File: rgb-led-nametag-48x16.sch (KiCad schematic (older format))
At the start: 1 part, among them J1 USB_C_Receptacle_USB2.0

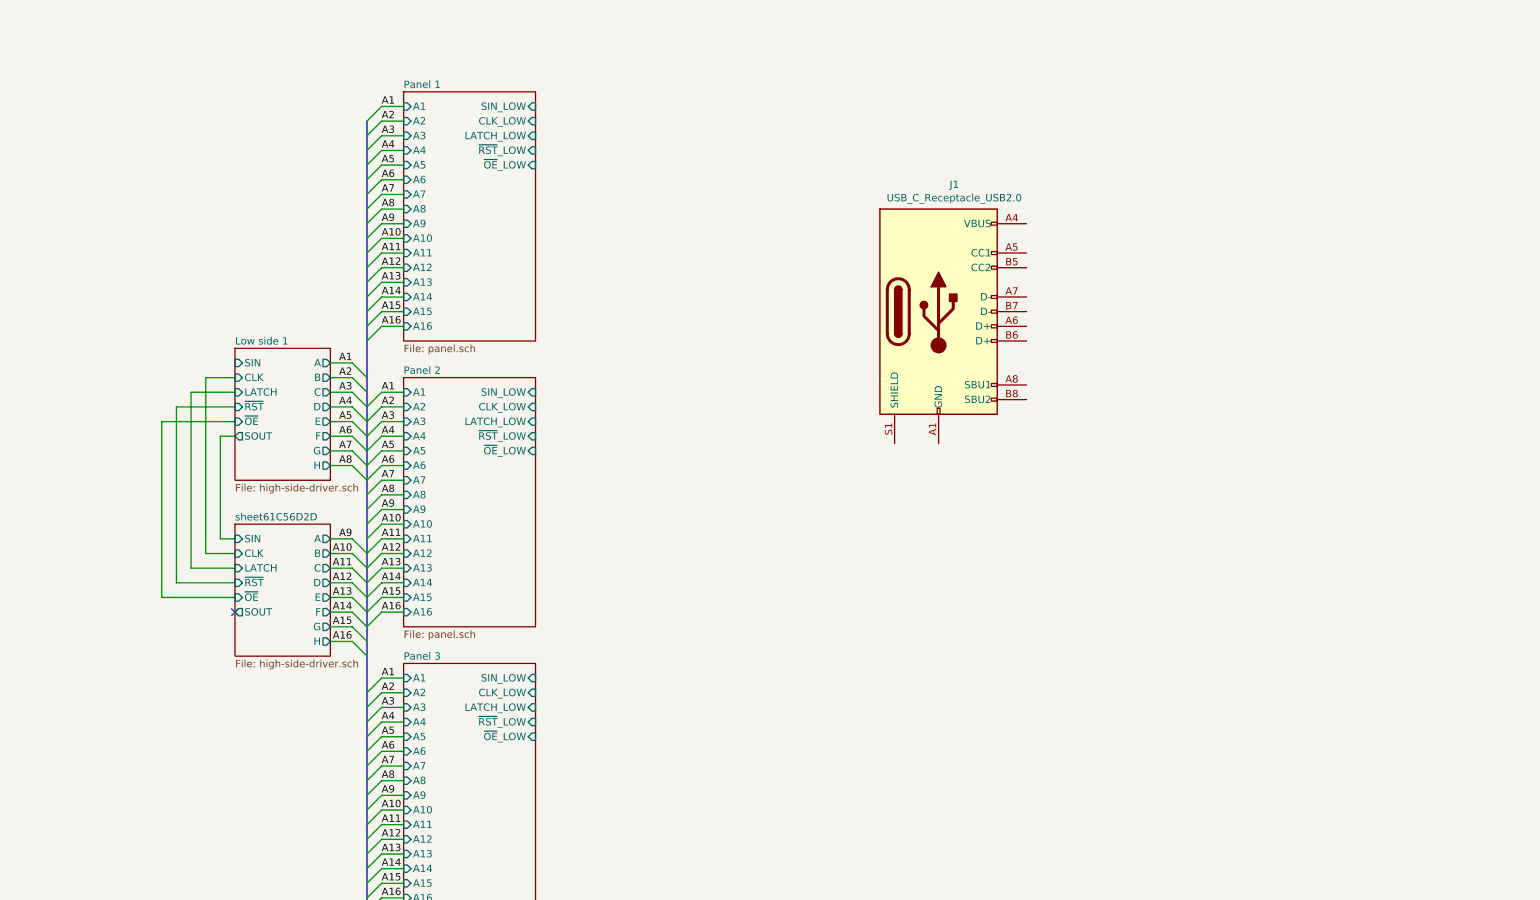
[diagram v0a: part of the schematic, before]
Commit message: Finish STM32 digital interface assignment
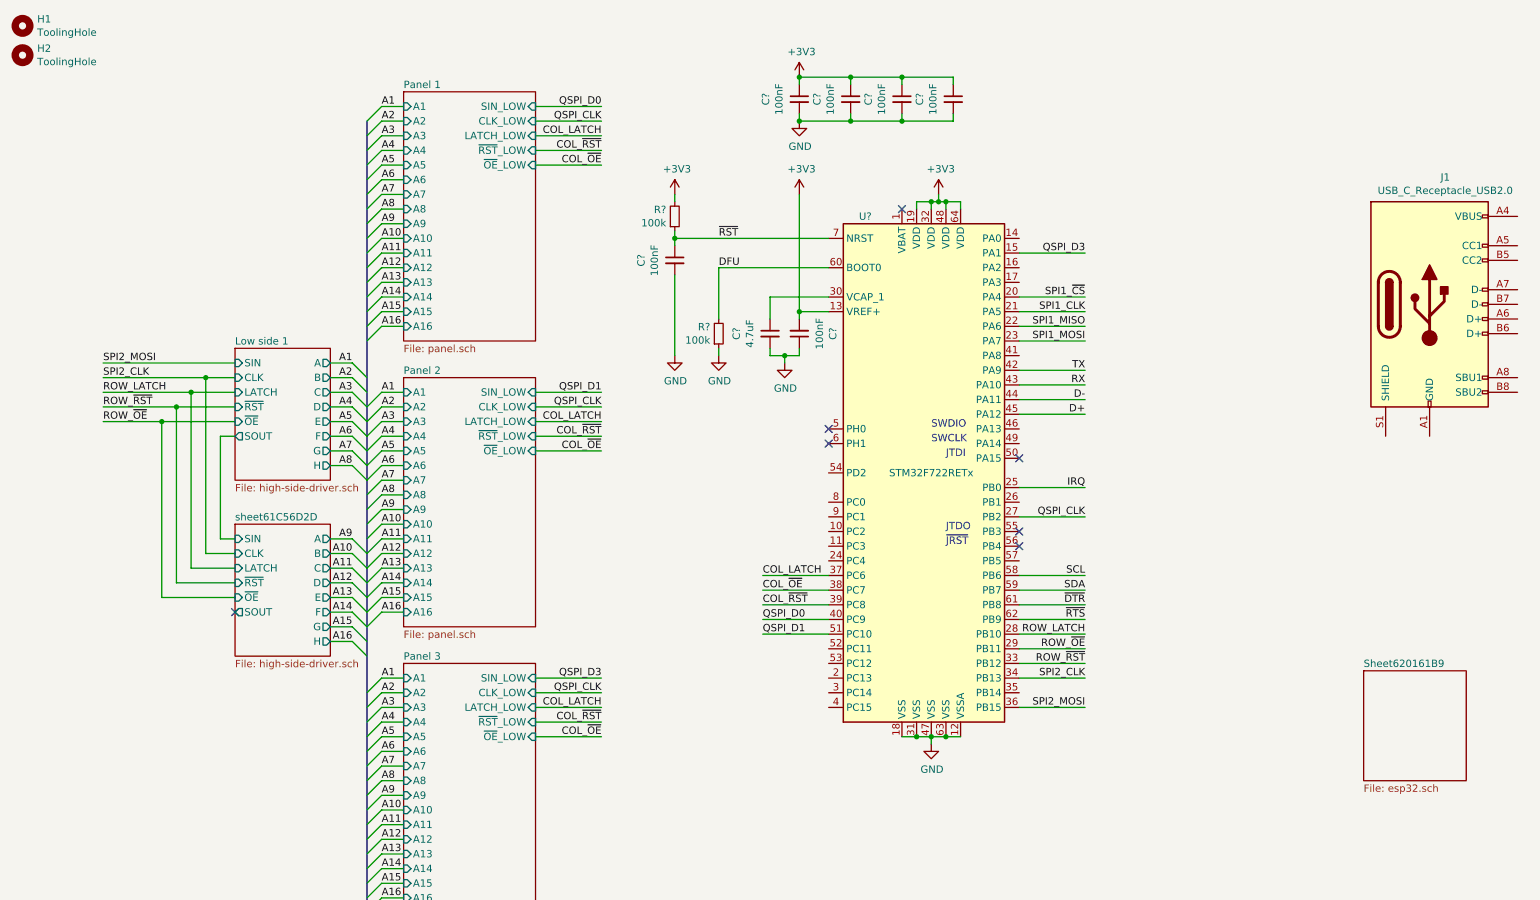
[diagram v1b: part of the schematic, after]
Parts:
- added C?: 4.7uF, Capacitor_SMD:C_0402_1005Metric, symbol Device:C_Small
- added C? (x6): 100nF, Capacitor_SMD:C_0402_1005Metric, symbol Device:C_Small
- added H1, H2: ToolingHole, ToolingHole:ToolingHole_JLCSMT, symbol Mechanical:MountingHole
- added R? (x2): 100k, Resistor_SMD:R_0402_1005Metric, symbol Device:R_Small
- added U?: STM32F722RETx, Package_QFP:LQFP-64_10x10mm_P0.5mm, symbol MCU_ST_STM32F7:STM32F722RETx
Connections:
- new net: C?.1, U?.30 (VCAP_1)
- new net +3V3: C?.1, C?.1, C?.1, C?.1, C?.2, R?.2, U?.13 (VREF+), U?.19 (VDD), U?.32 (VDD), U?.48 (VDD), U?.64 (VDD)
- new net COL_LATCH: U?.37 (PC6)
- new net COL_~OE: U?.38 (PC7)
- new net COL_~RST: U?.39 (PC8)
- new net D+: U?.45 (PA12)
- new net D-: U?.44 (PA11)
- new net DFU: R?.2, U?.60 (BOOT0)
- new net GND: C?.1, C?.2, C?.2, C?.2, C?.2, C?.2, C?.2, R?.1, U?.12 (VSSA), U?.18 (VSS), U?.31 (VSS), U?.47 (VSS), U?.63 (VSS)
- new net IRQ: U?.25 (PB0)
- new net QSPI_CLK: U?.27 (PB2)
- new net QSPI_D0: U?.40 (PC9)
- new net QSPI_D1: U?.51 (PC10)
- new net QSPI_D3: U?.15 (PA1)
- new net ROW_LATCH: U?.28 (PB10)
- new net ROW_~OE: U?.29 (PB11)
- new net ROW_~RST: U?.33 (PB12)
- new net RX: U?.43 (PA10)
- new net SCL: U?.58 (PB6)
- new net SDA: U?.59 (PB7)
- new net SPI1_CLK: U?.21 (PA5)
- new net SPI1_MISO: U?.22 (PA6)
- new net SPI1_MOSI: U?.23 (PA7)
- new net SPI1_~CS: U?.20 (PA4)
- new net SPI2_CLK: U?.34 (PB13)
- new net SPI2_MOSI: U?.36 (PB15)
- new net TX: U?.42 (PA9)
- new net ~DTR: U?.61 (PB8)
- new net ~RST: C?.1, R?.1, U?.7 (NRST)
- new net ~RTS: U?.62 (PB9)
- no-connect marks 1 -> 7
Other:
- note added: "JTDI"
- note added: "JTDO"
- note added: "SWCLK"
- note added: "SWDIO"
- note added: "~JRST"
- moved on the sheet: J1

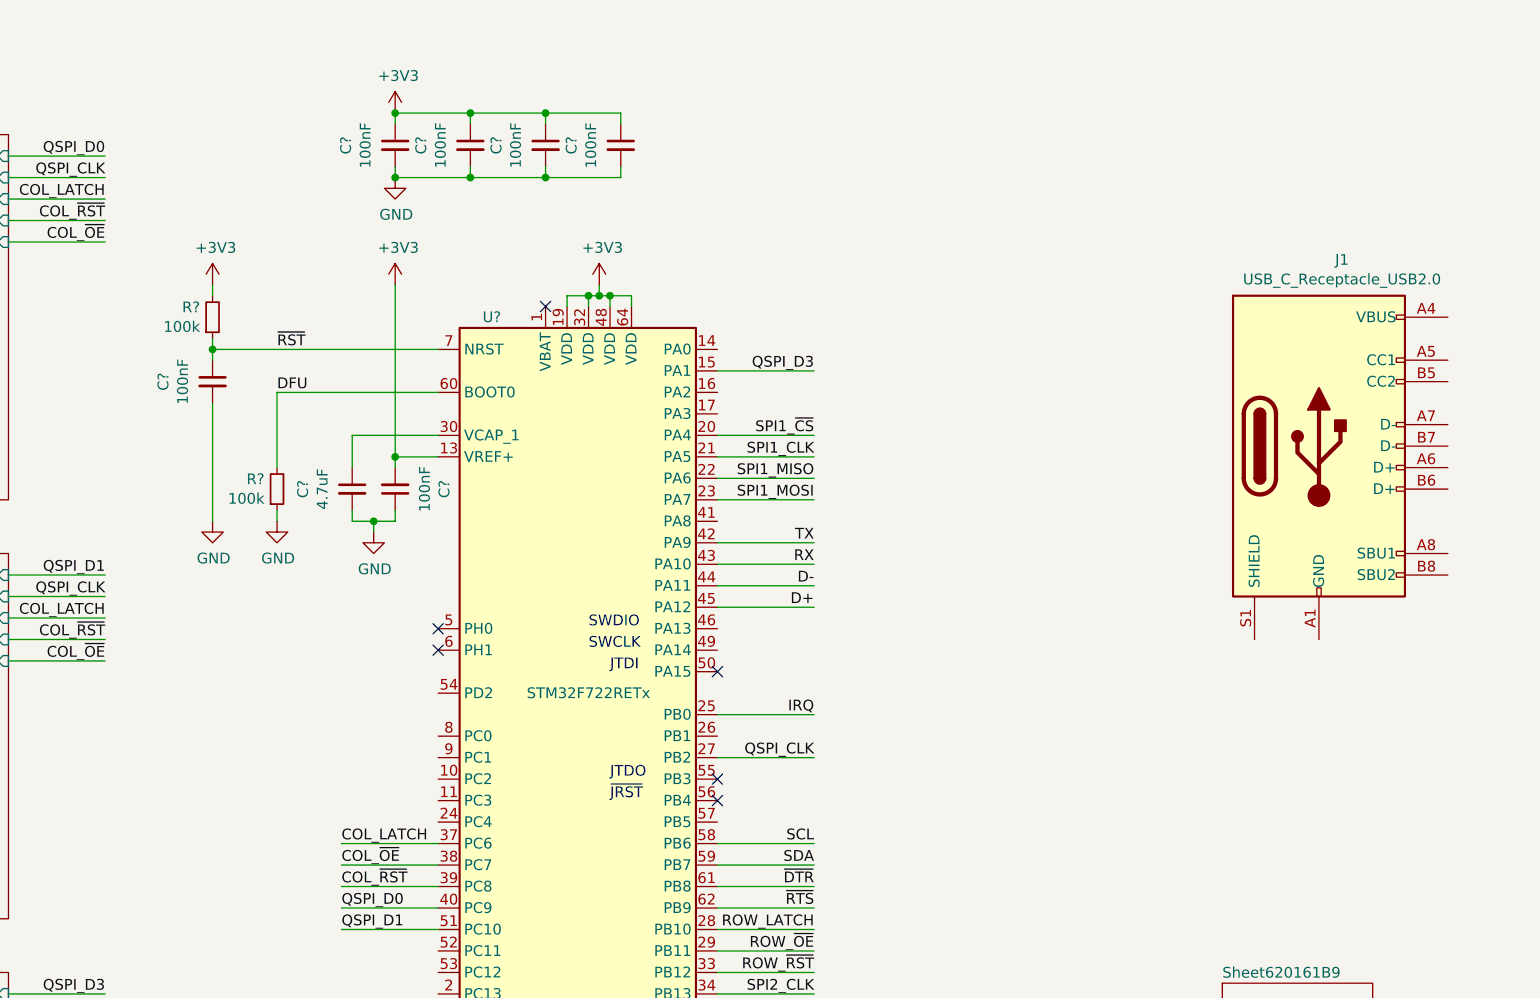
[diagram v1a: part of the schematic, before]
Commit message: Add multiplexing MCU and USB
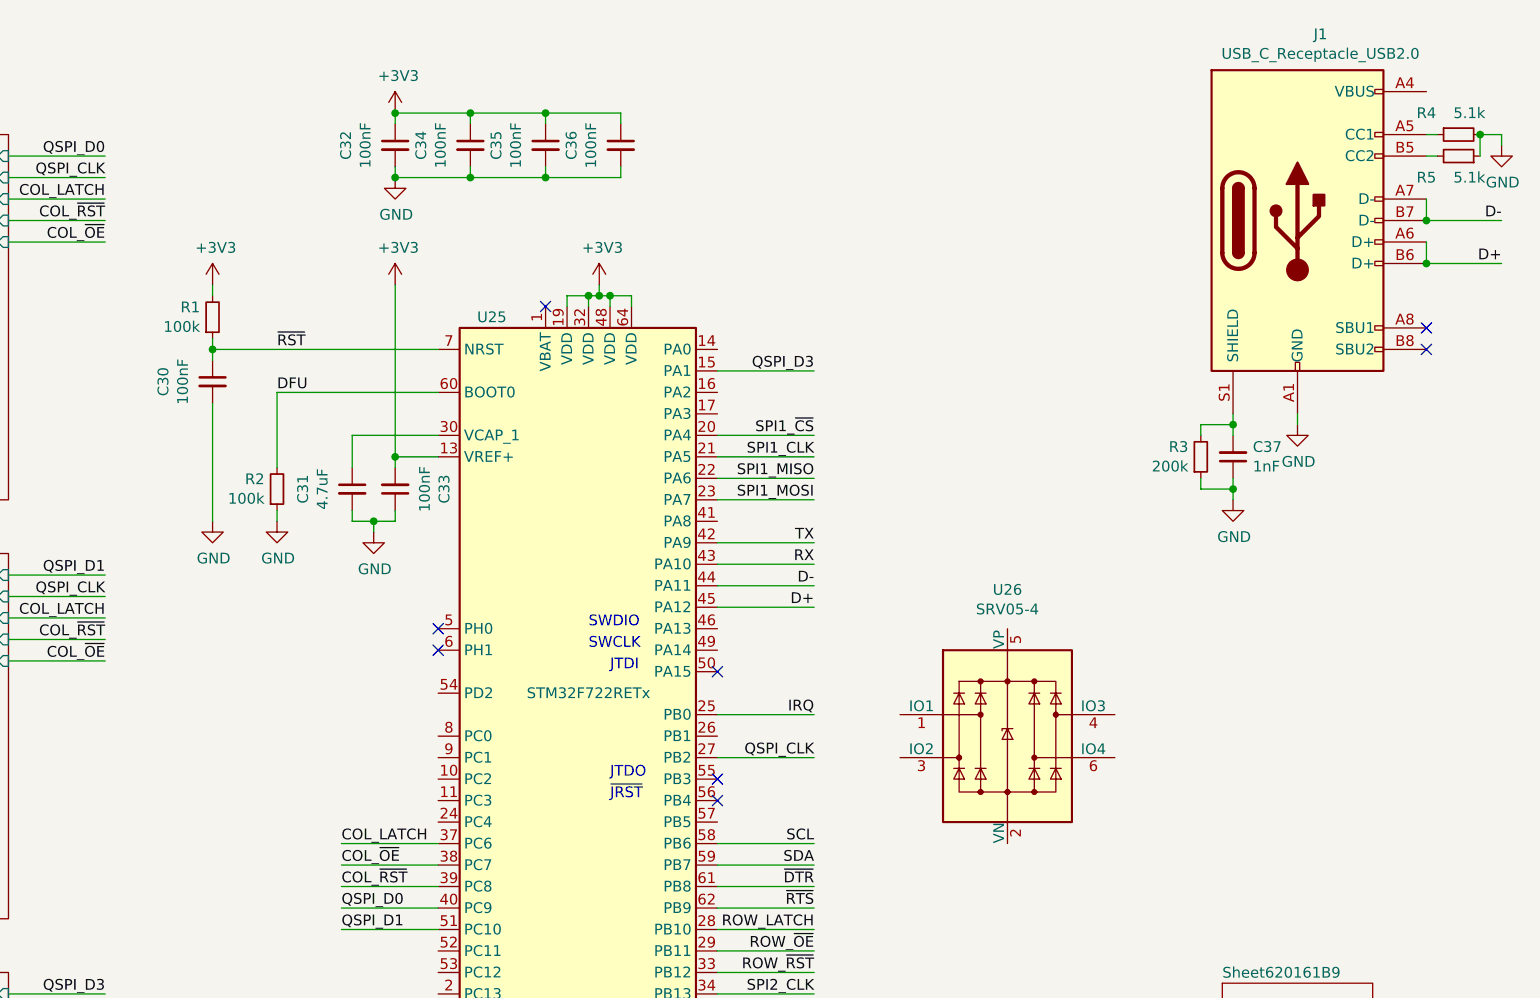
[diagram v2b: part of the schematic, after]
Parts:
- added C37: 1nF, Capacitor_SMD:C_1206_3216Metric, symbol Device:C_Small
- added R3: 200k, Resistor_SMD:R_0805_2012Metric, symbol Device:R_Small
- added R4, R5: 5.1k, Resistor_SMD:R_0402_1005Metric, symbol Device:R_Small
- added U26: SRV05-4, Package_TO_SOT_SMD:SOT-23-6, symbol Power_Protection:SRV05-4
- U25: renamed from U?; LCSC (none) -> C118207
- gave numbers to parts that had none: 9
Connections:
- net D+: now also J1.A6 (D+), J1.B6 (D+)
- net D-: now also J1.A7 (D-), J1.B7 (D-)
- net GND: now also J1.A1 (GND), J1.A12 (GND), J1.B1 (GND), J1.B12 (GND), C37.1, R3.1, R4.2, R5.1
- net at J1.A5 (CC1): now also R4.1
- net at J1.B5 (CC2): now also R5.2
- net at J1.S1 (SHIELD): now also C37.2, R3.2
- no-connect marks 7 -> 9
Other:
- moved on the sheet: J1

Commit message: Add tag connect programming/debug interface
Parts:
- added J?: TagConnect_TC2030_SWD, Connector:Tag-Connect_TC2030-IDC-NL_2x03_P1.27mm_Vertical, symbol Connector_TagConnect:TagConnect_TC2030_SWD
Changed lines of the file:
@@
 	2950 1250 2950 6650
 Connection ~ 9800 2700
+$Comp
+L Connector_TagConnect:TagConnect_TC2030_SWD J?
+U 1 1 620AEB39
+P 8650 2850
+F 0 "J?" H 8650 3175 50  0000 C CNN
+F 1 "TagConnect_TC2030_SWD" H 8650 3084 50  0000 C CNN
+F 2 "Connector:Tag-Connect_TC2030-IDC-NL_2x03_P1.27mm_Vertical" H 8650 2850 50  0001 C CNN
+F 3 "" H 8650 2850 50  0001 C CNN
+	1    8650 2850
+	1    0    0    -1
+$EndComp
 $EndSCHEMATC

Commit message: Add mounting pad for safety pin
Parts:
- added H?: MountingPad, MountingPad:MountingPad_20x5mm, symbol Mechanical:MountingHole_Pad
- added U?: TPS63001, Package_SON:Texas_DRC0010J_ThermalVias, symbol Regulator_Switching:TPS63001
- gave numbers to parts that had none: 1
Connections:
- net GND: now also H?.1
- new net: U?.11 (PGND), U?.3 (PGND)
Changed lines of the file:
@@
 Connection ~ 9800 2700
 $Comp
-L Connector_TagConnect:TagConnect_TC2030_SWD J?
+L Connector_TagConnect:TagConnect_TC2030_SWD J2
 U 1 1 620AEB39
 P 8650 2850
-F 0 "J?" H 8650 3175 50  0000 C CNN
+F 0 "J2" H 8650 3175 50  0000 C CNN
 F 1 "TagConnect_TC2030_SWD" H 8650 3084 50  0000 C CNN
 F 2 "Connector:Tag-Connect_TC2030-IDC-NL_2x03_P1.27mm_Vertical" H 8650 2850 50  0001 C CNN
@@
 	1    0    0    -1
 $EndComp
+$Comp
+L Regulator_Switching:TPS63001 U?
+U 1 1 620B2056
+P 12600 1900
+F 0 "U?" H 12600 2567 50  0000 C CNN
+F 1 "TPS63001" H 12600 2476 50  0000 C CNN
+F 2 "Package_SON:Texas_DRC0010J_ThermalVias" H 13450 1350 50  0001 C CNN
+F 3 "http://www.ti.com/lit/ds/symlink/tps63000.pdf" H 12300 2450 50  0001 C CNN
+	1    12600 1900
+	1    0    0    -1
+$EndComp
+$Comp
+L Mechanical:MountingHole_Pad H?
+U 1 1 620BC07C
+P 600 1050
+F 0 "H?" H 700 1099 50  0000 L CNN
+F 1 "MountingPad" H 700 1008 50  0000 L CNN
+F 2 "MountingPad:MountingPad_20x5mm" H 600 1050 50  0001 C CNN
+F 3 "~" H 600 1050 50  0001 C CNN
+	1    600  1050
+	1    0    0    -1
+$EndComp
+$Comp
+L power:GND #PWR?
+U 1 1 620BCEB0
+P 600 1150
+F 0 "#PWR?" H 600 900 50  0001 C CNN
+F 1 "GND" H 605 977 50  0000 C CNN
+F 2 "" H 600 1150 50  0001 C CNN
+F 3 "" H 600 1150 50  0001 C CNN
+	1    600  1150
+	1    0    0    -1
+$EndComp

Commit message: Make space for STM32
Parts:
- gave numbers to parts that had none: 2
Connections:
- net D+: now also U26.3 (IO2)
- net D-: now also U26.1 (IO1)
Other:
- moved on the sheet: U26
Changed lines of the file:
@@
 L Power_Protection:SRV05-4 U26
 U 1 1 61FD5228
-P 8750 3850
-F 0 "U26" H 8750 4531 50  0000 C CNN
-F 1 "SRV05-4" H 8750 4440 50  0000 C CNN
-F 2 "Package_TO_SOT_SMD:SOT-23-6" H 9450 3400 50  0001 C CNN
-F 3 "http://www.onsemi.com/pub/Collateral/SRV05-4-D.PDF" H 8750 3850 50  0001 C CNN
-F 4 "C85364" H 8750 3850 50  0001 C CNN "LCSC"
-	1    8750 3850
+P 9350 3900
+F 0 "U26" H 9350 4581 50  0000 C CNN
+F 1 "SRV05-4" H 9350 4490 50  0000 C CNN
+F 2 "Package_TO_SOT_SMD:SOT-23-6" H 10050 3450 50  0001 C CNN
+F 3 "http://www.onsemi.com/pub/Collateral/SRV05-4-D.PDF" H 9350 3900 50  0001 C CNN
+F 4 "C85364" H 9350 3900 50  0001 C CNN "LCSC"
+	1    9350 3900
 	1    0    0    -1
 $EndComp
@@
 Wire Wire Line
 	9800 2750 9800 2700
-Wire Bus Line
-	2950 1250 2950 6650
 Connection ~ 9800 2700
 $Comp
@@
 $EndComp
 $Comp
-L Regulator_Switching:TPS63001 U?
+L Regulator_Switching:TPS63001 U27
 U 1 1 620B2056
 P 12600 1900
-F 0 "U?" H 12600 2567 50  0000 C CNN
+F 0 "U27" H 12600 2567 50  0000 C CNN
 F 1 "TPS63001" H 12600 2476 50  0000 C CNN
 F 2 "Package_SON:Texas_DRC0010J_ThermalVias" H 13450 1350 50  0001 C CNN
@@
 $EndComp
 $Comp
-L Mechanical:MountingHole_Pad H?
+L Mechanical:MountingHole_Pad H3
 U 1 1 620BC07C
 P 600 1050
-F 0 "H?" H 700 1099 50  0000 L CNN
+F 0 "H3" H 700 1099 50  0000 L CNN
 F 1 "MountingPad" H 700 1008 50  0000 L CNN
 F 2 "MountingPad:MountingPad_20x5mm" H 600 1050 50  0001 C CNN
@@
 $EndComp
 $Comp
-L power:GND #PWR?
+L power:GND #PWR0178
 U 1 1 620BCEB0
 P 600 1150
-F 0 "#PWR?" H 600 900 50  0001 C CNN
+F 0 "#PWR0178" H 600 900 50  0001 C CNN
 F 1 "GND" H 605 977 50  0000 C CNN
 F 2 "" H 600 1150 50  0001 C CNN
@@
 	1    0    0    -1
 $EndComp
+Wire Wire Line
+	8850 3800 8650 3800
+Text Label 8650 3800 0    50   ~ 0
+D-
+Wire Wire Line
+	8850 4000 8650 4000
+Text Label 8650 4000 0    50   ~ 0
+D+
+Wire Bus Line
+	2950 1250 2950 6650
 $EndSCHEMATC
